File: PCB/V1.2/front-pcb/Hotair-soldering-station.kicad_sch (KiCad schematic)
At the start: 24 parts, among them J1 Conn_01x03, J2 main-board-conn, J3 hot_on, SW1 HOTAIR_UP, SW2 HOTAIR_DOWN, SW3 SIRON_UP, SW4 SIRON_DOWN, SW5 FAN_UP, SW6 FAN_DOWN, SW7 MENU_UP, SW8 MENU_DOWN, SW9 MENU_OK

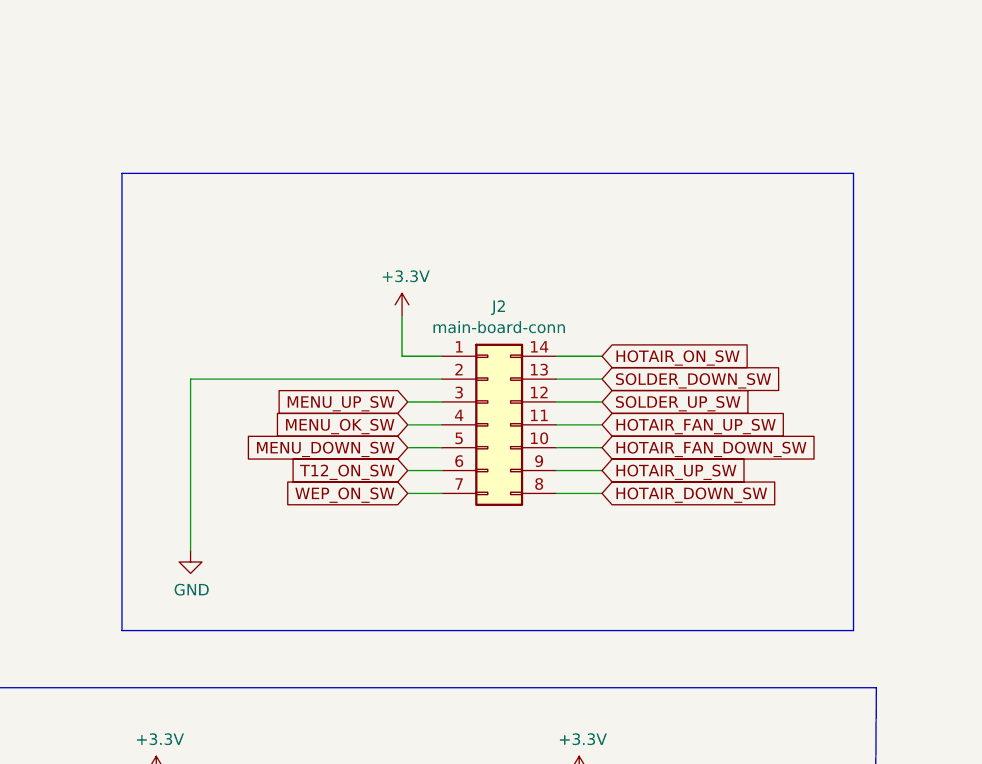
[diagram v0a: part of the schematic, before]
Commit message: T12 and WEP tests done
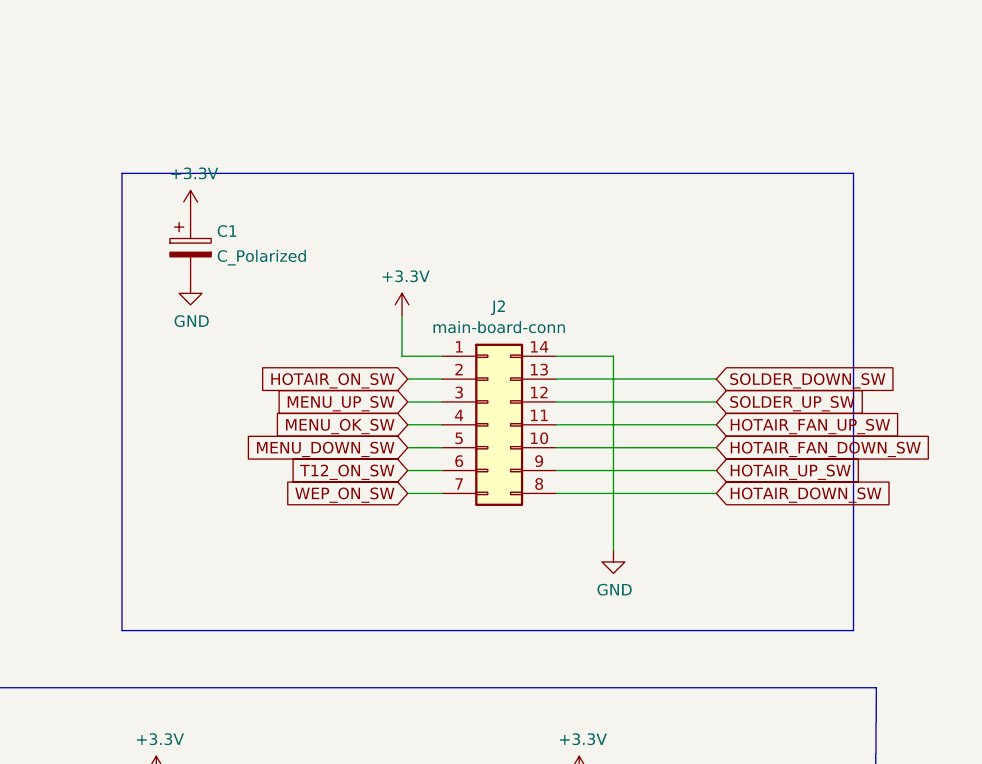
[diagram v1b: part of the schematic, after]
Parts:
- added C1: C_Polarized, Capacitors_Tantalum_SMD:CP_Tantalum_Case-B_EIA-3528-21_Hand, symbol Device:C_Polarized
- J2: footprint My-Footprints:Con-01x14 -> My-Footprints:IDC-Header_2x07_P2.54mm_Vertical
- SW1, SW2, SW3, SW4, SW5, SW6: footprint Switches:TACTILE_SWITCH_PTH_12MM -> My-Footprints:TACTILE_SWITCH_PTH_12MM
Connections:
- net +3V3: now also C1.1
- net GND: now also J2.14 (Pin_14), C1.2; no longer J2.2 (Pin_2)
- net HOTAIR_ON_SW: now also J2.2 (Pin_2); no longer J2.14 (Pin_14)

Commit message: Main and front PCB schematic rearrangement.
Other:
- note added: "HOTAIR TACT SWITCHES"
- note added: "MAIN CONNECTOR"
- note added: "MENU TACT SWITCHES"
- note added: "SOLDERING IRONS TACT SWITCHES"
- moved on the sheet: C1, J1, J2, J3, R1, R2, R23, R24, R25, R26, R27, R28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

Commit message: Front panel done
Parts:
- C1: value C_Polarized -> 10u
- J2: renamed from J1; value Conn_01x03 -> SOLDER_ON_SW
- J3: value hot_on -> HOTAIR_ON_SW
- SW1: renamed from SW7; value MENU_UP -> MENU_RIGHT
- SW2: renamed from SW8; value MENU_DOWN -> MENU_LEFT
- SW4: renamed from SW3; value SIRON_UP -> SOLDER_UP_TEMP
- SW5: renamed from SW4; value SIRON_DOWN -> SOLDER_DOWN_TEMP
- SW8: renamed from SW1; value HOTAIR_UP -> HOTAIR_UP_TEMP
- SW9: renamed from SW2; value HOTAIR_DOWN -> HOTAIR_DOWN_TEMP
- renumbered J2 to J1, R30 to R10, R25 to R11, R27 to R12, R24 to R4, R28 to R5, R26 to R6, R4 to R7, R29 to R8, R23 to R9, SW9 to SW3, SW5 to SW6, SW6 to SW7
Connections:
- net MENU_DOWN_SW renamed MENU_LEFT_SW
- net MENU_UP_SW renamed MENU_RIGHT_SW
